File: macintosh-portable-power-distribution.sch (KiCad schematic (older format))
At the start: 23 parts, among them Q1 IRF9Z30, Q10 IRF9020, Q11 IRF9020, Q13 IRF9020, Q14 IRF9Z30, Q15 IRF9Z30, Q16 IRF9Z30, Q2 IRF9020, Q20 IRF9Z30, Q24 702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

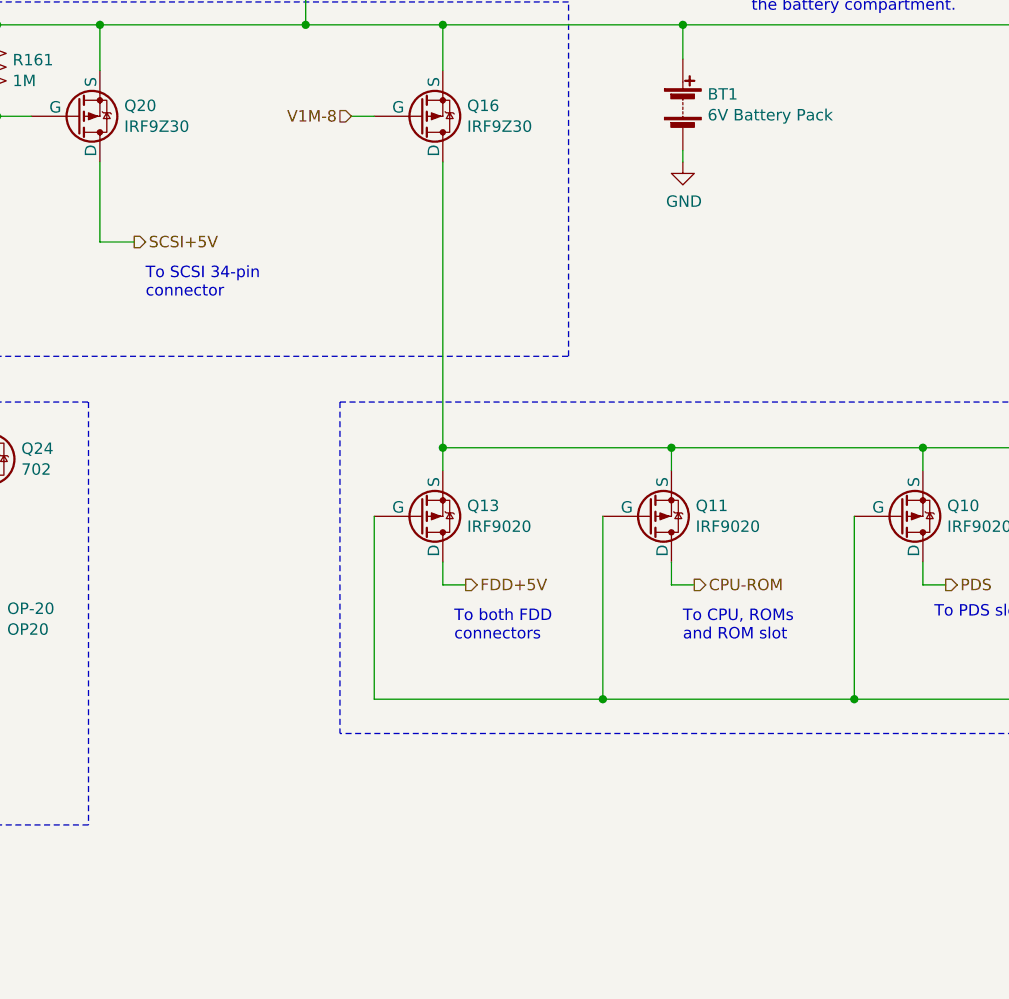
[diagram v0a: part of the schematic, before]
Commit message: Added secondary stage output and RAM output
Signed-off-by: Pawel Pieczul <pieczul@gmail.com>
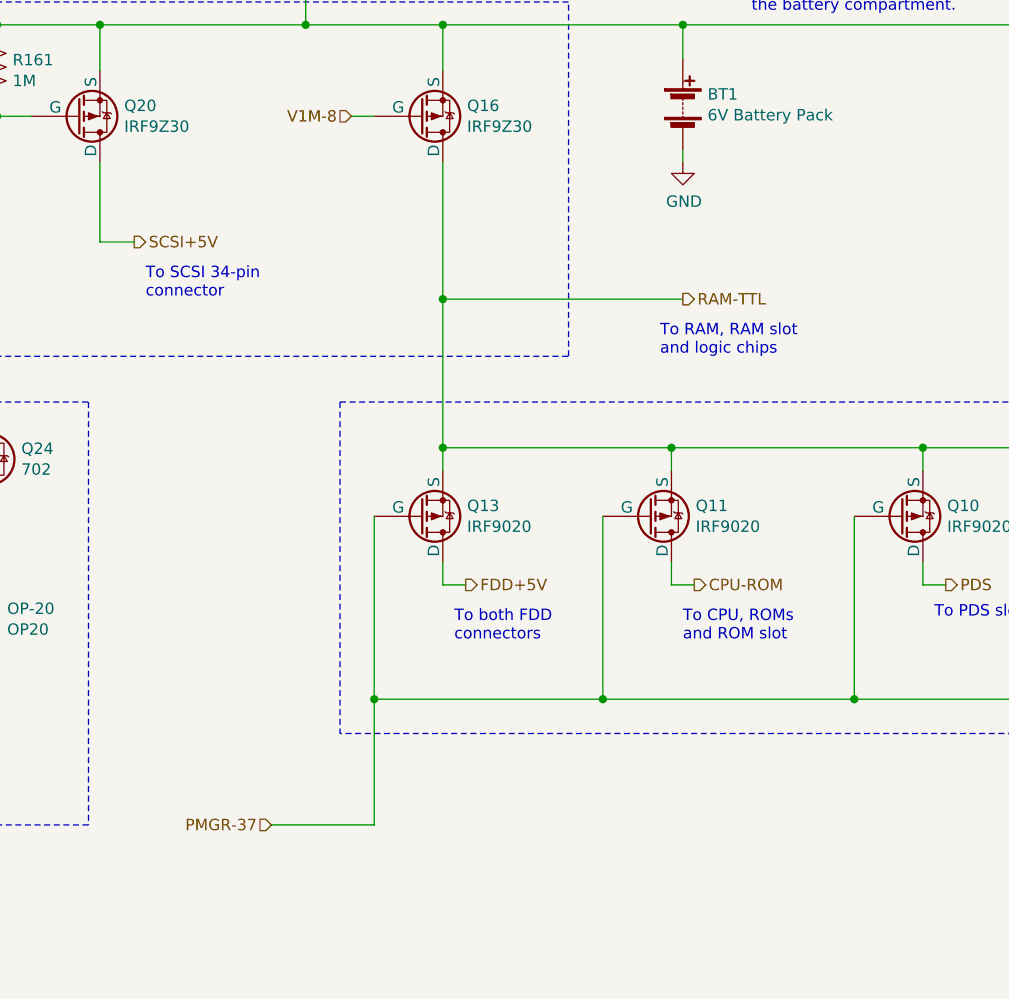
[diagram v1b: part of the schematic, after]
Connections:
- net RAM-TTL: now reaches Q10.3 (S), Q11.3 (S), Q13.3 (S), Q16.2 (D), Q2.3 (S), Q4.3 (S)
- net PMGR-37: now reaches Q10.1 (G), Q11.1 (G), Q13.1 (G), Q4.1 (G)
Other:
- note added: "To RAM, RAM slot\nand logic chips"
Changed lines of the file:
@@
 Title "Macintosh Portable Power Distribution"
 Date "2019-05-22"
-Rev "0.1"
+Rev "0.11"
 Comp "https://oldcrap.org"
 Comment1 ""
@@
 	5750 4650 5750 6100
 Wire Wire Line
-	6200 3600 6200 4850
+	6200 3600 6200 4200
 $Comp
 L Device:Battery BT1
@@
 Text Notes 900  7450 0    50   ~ 0
 V1M - voltage control module, location 1-4M\nPMGR - power management chip, location H15
+Text HLabel 7250 4200 2    50   Output ~ 0
+RAM-TTL
+Wire Wire Line
+	7250 4200 6200 4200
+Connection ~ 6200 4200
+Wire Wire Line
+	6200 4200 6200 4850
+Text Notes 7150 4450 0    50   ~ 0
+To RAM, RAM slot\nand logic chips
+Text HLabel 5450 6500 0    50   Input ~ 0
+PMGR-37
+Wire Wire Line
+	5450 6500 5900 6500
+Wire Wire Line
+	5900 6500 5900 5950
+Connection ~ 5900 5950
 $EndSCHEMATC

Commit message: Added V1M module.
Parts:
- added C16: 100uF, symbol Device:CP1
- added C26, C?: 47uF, symbol Device:CP1
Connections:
- net V1M-41: now also C16.2
- net V1M-51: now also C26.1
- new net: C26.2, C?.2
- new net V1M-39: C16.1
- new net V1M-52: C?.1
- no-connect marks 0 -> 2
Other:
- moved on the sheet: R160
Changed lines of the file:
@@
 $Descr A4 11693 8268
 encoding utf-8
-Sheet 2 3
+Sheet 2 4
 Title "Macintosh Portable Power Distribution"
 Date "2019-05-22"
@@
 L Device:R_US R160
 U 1 1 5CE60BCC
-P 2700 5700
-F 0 "R160" V 2495 5700 50  0000 C CNN
-F 1 "75k" V 2586 5700 50  0000 C CNN
-F 2 "" V 2740 5690 50  0001 C CNN
-F 3 "~" H 2700 5700 50  0001 C CNN
-	1    2700 5700
+P 2850 5700
+F 0 "R160" V 2645 5700 50  0000 C CNN
+F 1 "75k" V 2736 5700 50  0000 C CNN
+F 2 "" V 2890 5690 50  0001 C CNN
+F 3 "~" H 2850 5700 50  0001 C CNN
+	1    2850 5700
 	0    1    1    0
 $EndComp
 Wire Wire Line
-	2850 5700 3200 5700
+	3000 5700 3200 5700
 Connection ~ 3200 5700
 Text HLabel 2400 5700 0    50   Input ~ 0
 V1M-51
 Wire Wire Line
-	2550 5700 2400 5700
+	2700 5700 2550 5700
 Wire Wire Line
 	3200 6000 3200 6050
@@
 Wire Notes Line
 	1850 6500 1850 4650
-Text Notes 1950 6400 0    50   ~ 0
+Text Notes 3650 6400 0    50   ~ 0
 SCSI power enable logic
 Text Notes 4900 4200 0    50   ~ 0
@@
 	5900 6500 5900 5950
 Connection ~ 5900 5950
+Text HLabel 2400 7050 0    50   Input ~ 0
+V1M-52
+$Comp
+L Device:CP1 C26
+U 1 1 5CEA6F81
+P 2550 6050
+F 0 "C26" H 2665 6096 50  0000 L CNN
+F 1 "47uF" H 2665 6005 50  0000 L CNN
+F 2 "" H 2550 6050 50  0001 C CNN
+F 3 "~" H 2550 6050 50  0001 C CNN
+	1    2550 6050
+	1    0    0    -1
+$EndComp
+Wire Wire Line
+	2550 5900 2550 5700
+Connection ~ 2550 5700
+Wire Wire Line
+	2550 5700 2400 5700
+$Comp
+L Device:CP1 C?
+U 1 1 5CEB228F
+P 2550 6750
+F 0 "C?" H 2435 6704 50  0000 R CNN
+F 1 "47uF" H 2435 6795 50  0000 R CNN
+F 2 "" H 2550 6750 50  0001 C CNN
+F 3 "~" H 2550 6750 50  0001 C CNN
+	1    2550 6750
+	-1   0    0    1
+$EndComp
+Wire Wire Line
+	2550 7050 2400 7050
+Wire Wire Line
+	2550 6900 2550 7050
+Wire Wire Line
+	2550 6600 2550 6200
+Text HLabel 9550 1400 2    50   Output ~ 0
+V1M-39
+Text HLabel 9550 1950 2    50   Output ~ 0
+V1M-41
+$Comp
+L Device:CP1 C16
+U 1 1 5CF544A6
+P 9150 1700
+F 0 "C16" H 9265 1746 50  0000 L CNN
+F 1 "100uF" H 9265 1655 50  0000 L CNN
+F 2 "" H 9150 1700 50  0001 C CNN
+F 3 "~" H 9150 1700 50  0001 C CNN
+	1    9150 1700
+	1    0    0    -1
+$EndComp
+Wire Wire Line
+	9150 1550 9150 1400
+Wire Wire Line
+	9150 1400 9550 1400
+Wire Wire Line
+	9150 1850 9150 1950
+Wire Wire Line
+	9150 1950 9550 1950
+NoConn ~ 3950 5900
+NoConn ~ 4050 5900
 $EndSCHEMATC

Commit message: Finished V1M, more references on other sheets.
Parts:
- added C107: 1A4, symbol Device:C
- added C108, C109: 1A5, symbol Device:C
- added Q8: P2A, symbol Device:Q_PNP_BCE
- added Q9: 702, Package_TO_SOT_SMD:TO-252-3_TabPin2, symbol Transistor_FET:IRF9020
- added R101: 100k, symbol Device:R_US
- added R151: 1k, symbol Device:R_US
- added R158, R159: 2.2k, symbol Device:R_US
- C110: value ? -> 1A4
- Q25: value Q_NPN_BCE -> U92
- gave numbers to parts that had none: 1
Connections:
- net GND: now also C107.2, C108.2, C109.2
- net RAM-TTL: now also Q8.3 (E)
- net V1M-25: now also R159.2
- net at Q2.1 (G): now also R26.2; no longer R26.1
- net SERIAL renamed SERIAL-VCC
- new net: C109.1, R158.2, R159.1
- new net: Q8.2 (C), Q9.1 (G), R101.1
- new net: Q8.1 (B), R26.1
- new net J21-31: C107.1, R151.1
- new net J9-10: Q9.3 (S), R101.2
- new net SERIAL-VEE: Q9.2 (D)
- new net V1M-16: C108.1, R158.1
- new net V1M-62: R151.2
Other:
- note added: "Modem\npin 10\n"
- note added: "To 26LS3x (Vcc)"
- note added: "To 26LS3x (Vee)"
- note removed: "?"
- note removed: "To 26LS3x chips\n(ADB, serial I/O)"
- moved on the sheet: BT1, BT2, C110, C16, Q1, Q2, R157

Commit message: Symbol library cleanup
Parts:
- added C102, C103: 1A4, symbol Device:C
- added R147: 100k, symbol Device:R_US
- Q10, Q11, Q13, Q2, Q4: symbol Transistor_FET:IRF9020 -> macintosh-portable:IRF9020
- Q24: symbol Transistor_FET:702 -> macintosh-portable:702
- Q9: symbol Transistor_FET:IRF9020 -> macintosh-portable:702
- renumbered C16 to C18
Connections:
- net labels added: PMGR-45, PMGR-55, PMGR-56, V1M-29, V1M-31, V1M-37, V1M-40
- net labels removed: V1M-39
- wire segments 124 -> 138
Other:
- moved on the sheet: C107, C18, R151

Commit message: Progress on PMGR chip
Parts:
- removed C102, C103, C107: 1A4, symbol Device:C
- removed C18: 100uF, symbol Device:CP1
- removed R147: 100k, symbol Device:R_US
- removed R151: 1k, symbol Device:R_US
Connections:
- net labels added: PMGR-P0-2, PMGR-P0-7, PMGR-VCC
- net labels removed: J21-31, PMGR-37, PMGR-42, PMGR-45, PMGR-52, PMGR-55, PMGR-56, V1M-29, V1M-31, V1M-37, V1M-40, V1M-62
- wire segments 138 -> 116
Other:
- note added: "Enable power to\nRAM, RAM slot, \nlogic chips and PMGR"
- note removed: "To RAM, RAM slot\nand logic chips"
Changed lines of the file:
@@
 $Descr A4 11693 8268
 encoding utf-8
-Sheet 2 5
+Sheet 5 5
 Title "Macintosh Portable Power Distribution"
-Date "2019-05-27"
-Rev "0.12"
+Date "2019-06-08"
+Rev "0.13"
 Comp "https://oldcrap.org"
 Comment1 "Author: Pawel Pieczul"
@@
 V1M-51
 Wire Wire Line
-	2700 5700 2550 5700
-Wire Wire Line
 	3200 6000 3200 6050
 $Comp
@@
 	2850 5100 2900 5100
 Text HLabel 2400 5100 0    50   Input ~ 0
-PMGR-42
+PMGR-P0-2
 Wire Wire Line
 	2400 5100 2550 5100
@@
 V1M - voltage control module, location 1-4M\nPMGR - power management chip, location H15
 Text HLabel 5450 6500 0    50   Input ~ 0
-PMGR-37
+PMGR-P0-7
 Wire Wire Line
 	5450 6500 5900 6500
@@
 	5900 6500 5900 5950
 Connection ~ 5900 5950
-Text HLabel 2400 7050 0    50   Input ~ 0
-V1M-52
-$Comp
-L Device:CP1 C26
-U 1 1 5CEA6F81
-P 2550 6050
-F 0 "C26" H 2665 6096 50  0000 L CNN
-F 1 "47uF" H 2665 6005 50  0000 L CNN
-F 2 "" H 2550 6050 50  0001 C CNN
-F 3 "~" H 2550 6050 50  0001 C CNN
-	1    2550 6050
-	1    0    0    -1
-$EndComp
-Wire Wire Line
-	2550 5900 2550 5700
-Connection ~ 2550 5700
-Wire Wire Line
-	2550 5700 2400 5700
-$Comp
-L Device:CP1 C25
-U 1 1 5CEB228F
-P 2550 6750
-F 0 "C25" H 2435 6704 50  0000 R CNN
-F 1 "47uF" H 2435 6795 50  0000 R CNN
-F 2 "" H 2550 6750 50  0001 C CNN
-F 3 "~" H 2550 6750 50  0001 C CNN
-	1    2550 6750
-	-1   0    0    1
-$EndComp
-Wire Wire Line
-	2550 7050 2400 7050
-Wire Wire Line
-	2550 6900 2550 7050
-Wire Wire Line
-	2550 6600 2550 6200
 NoConn ~ 3950 5900
 NoConn ~ 4050 5900
@@
 Wire Wire Line
 	5600 1950 6000 1950
-$Comp
-L Device:R_US R?
-U 1 1 5DEE1891
-P 9500 900
-AR Path="/5DD4174A/5DEE1891" Ref="R?"  Part="1"
-AR Path="/5CE45908/5DEE1891" Ref="R151"  Part="1"
-F 0 "R151" V 9295 900 50  0000 C CNN
-F 1 "1k" V 9386 900 50  0000 C CNN
-F 2 "" V 9540 890 50  0001 C CNN
-F 3 "~" H 9500 900 50  0001 C CNN
-	1    9500 900
-	0    1    1    0
-$EndComp
-Text HLabel 9250 900  0    50   Input ~ 0
-V1M-62
-Wire Wire Line
-	9250 900  9350 900
-$Comp
-L Device:C C?
-U 1 1 5DEE8ED4
-P 9750 1050
-AR Path="/5DD4174A/5DEE8ED4" Ref="C?"  Part="1"
-AR Path="/5CE45908/5DEE8ED4" Ref="C107"  Part="1"
-F 0 "C107" H 9865 1096 50  0000 L CNN
-F 1 "1A4" H 9865 1005 50  0000 L CNN
-F 2 "" H 9788 900 50  0001 C CNN
-F 3 "~" H 9750 1050 50  0001 C CNN
-	1    9750 1050
-	1    0    0    -1
-$EndComp
-$Comp
-L power:GND #PWR?
-U 1 1 5DEE97A8
-P 9750 1200
-AR Path="/5DD4174A/5DEE97A8" Ref="#PWR?"  Part="1"
-AR Path="/5CE45908/5DEE97A8" Ref="#PWR?"  Part="1"
-F 0 "#PWR?" H 9750 950 50  0001 C CNN
-F 1 "GND" H 9755 1027 50  0000 C CNN
-F 2 "" H 9750 1200 50  0001 C CNN
-F 3 "" H 9750 1200 50  0001 C CNN
-	1    9750 1200
-	1    0    0    -1
-$EndComp
-Wire Wire Line
-	9650 900  9750 900
-Text HLabel 10500 900  2    50   Output ~ 0
-J21-31
-Wire Wire Line
-	9750 900  10200 900
-Connection ~ 9750 900
-Text HLabel 10500 1150 2    50   Output ~ 0
-PMGR-52
-Wire Wire Line
-	10200 900  10200 1150
-Wire Wire Line
-	10200 1150 10500 1150
-Connection ~ 10200 900
-Wire Wire Line
-	10200 900  10500 900
 Text HLabel 9600 3550 0    50   Input ~ 0
 V1M-33
@@
 Wire Notes Line
 	1850 4450 6750 4450
-Text Notes 7000 4550 0    50   ~ 0
-To RAM, RAM slot\nand logic chips
+Text Notes 7150 4600 0    50   ~ 0
+Enable power to\nRAM, RAM slot, \nlogic chips and PMGR
 Wire Wire Line
 	7250 3900 7050 3900
@@
 Text HLabel 3000 3650 0    50   Input ~ 0
 V1M-41
-Wire Wire Line
-	10100 2250 10500 2250
-Wire Wire Line
-	10100 2150 10100 2250
-Wire Wire Line
-	10100 1700 10500 1700
-Wire Wire Line
-	10100 1850 10100 1700
-$Comp
-L Device:CP1 C18
-U 1 1 5CF544A6
-P 10100 2000
-F 0 "C18" H 10215 2046 50  0000 L CNN
-F 1 "100uF" H 10215 1955 50  0000 L CNN
-F 2 "" H 10100 2000 50  0001 C CNN
-F 3 "~" H 10100 2000 50  0001 C CNN
-	1    10100 2000
-	1    0    0    -1
-$EndComp
-Text HLabel 10500 2250 2    50   Output ~ 0
-V1M-31
-Text HLabel 10500 1700 2    50   Output ~ 0
-V1M-29
-$Comp
-L Device:R_US R147
-U 1 1 5D12FA45
-P 3850 2200
-F 0 "R147" V 3645 2200 50  0000 C CNN
-F 1 "100k" V 3736 2200 50  0000 C CNN
-F 2 "" V 3890 2190 50  0001 C CNN
-F 3 "~" H 3850 2200 50  0001 C CNN
-	1    3850 2200
-	-1   0    0    1
-$EndComp
-Text HLabel 4100 1950 2    50   Output ~ 0
-V1M-40
-$Comp
-L Device:C C102
-U 1 1 5D1473B8
-P 3450 2200
-F 0 "C102" H 3565 2246 50  0000 L CNN
-F 1 "1A4" H 3565 2155 50  0000 L CNN
-F 2 "" H 3488 2050 50  0001 C CNN
-F 3 "~" H 3450 2200 50  0001 C CNN
-	1    3450 2200
-	1    0    0    -1
-$EndComp
-Wire Wire Line
-	3850 2050 3850 1950
-Wire Wire Line
-	3850 1950 4100 1950
-Wire Wire Line
-	3450 2050 3450 1950
-Wire Wire Line
-	3450 1950 3850 1950
-Connection ~ 3850 1950
-$Comp
-L power:GND #PWR?
-U 1 1 5D15188C
-P 3850 2350
-AR Path="/5DD4174A/5D15188C" Ref="#PWR?"  Part="1"
-AR Path="/5CE45908/5D15188C" Ref="#PWR?"  Part="1"
-F 0 "#PWR?" H 3850 2100 50  0001 C CNN
-F 1 "GND" H 3855 2177 50  0000 C CNN
-F 2 "" H 3850 2350 50  0001 C CNN
-F 3 "" H 3850 2350 50  0001 C CNN
-	1    3850 2350
-	1    0    0    -1
-$EndComp
-$Comp
-L power:GND #PWR?
-U 1 1 5D152016
-P 3450 2350
-AR Path="/5DD4174A/5D152016" Ref="#PWR?"  Part="1"
-AR Path="/5CE45908/5D152016" Ref="#PWR?"  Part="1"
-F 0 "#PWR?" H 3450 2100 50  0001 C CNN
-F 1 "GND" H 3455 2177 50  0000 C CNN
-F 2 "" H 3450 2350 50  0001 C CNN
-F 3 "" H 3450 2350 50  0001 C CNN
-	1    3450 2350
-	1    0    0    -1
-$EndComp
-Text HLabel 8250 900  2    50   Input ~ 0
-V1M-37
-$Comp
-L Device:C C103
-U 1 1 5D16A202
-P 8050 1150
-F 0 "C103" H 8165 1196 50  0000 L CNN
-F 1 "1A4" H 8165 1105 50  0000 L CNN
-F 2 "" H 8088 1000 50  0001 C CNN
-F 3 "~" H 8050 1150 50  0001 C CNN
-	1    8050 1150
-	1    0    0    -1
-$EndComp
-$Comp
-L power:GND #PWR?
-U 1 1 5D16AB1B
-P 8050 1300
-AR Path="/5DD4174A/5D16AB1B" Ref="#PWR?"  Part="1"
-AR Path="/5CE45908/5D16AB1B" Ref="#PWR?"  Part="1"
-F 0 "#PWR?" H 8050 1050 50  0001 C CNN
-F 1 "GND" H 8055 1127 50  0000 C CNN
-F 2 "" H 8050 1300 50  0001 C CNN
-F 3 "" H 8050 1300 50  0001 C CNN
-	1    8050 1300
-	1    0    0    -1
-$EndComp
-Wire Wire Line
-	8250 900  8050 900
-Wire Wire Line
-	8050 900  8050 1000
-Text HLabel 8300 3900 2    50   Output ~ 0
-PMGR-45
-Text HLabel 8300 4050 2    50   Output ~ 0
-PMGR-55
-Text HLabel 8300 4200 2    50   Output ~ 0
-PMGR-56
+Text HLabel 8250 4350 2    50   Output ~ 0
+PMGR-VCC
 Connection ~ 7050 4050
 Connection ~ 7050 4200
@@
 Wire Wire Line
 	7050 3900 7050 4050
-Wire Wire Line
-	7050 4350 8050 4350
-Wire Wire Line
-	8050 4350 8050 4200
-Wire Wire Line
-	8050 4200 8300 4200
 Connection ~ 7050 4350
 Wire Wire Line
-	8050 4200 8050 4050
-Wire Wire Line
-	8050 4050 8300 4050
-Connection ~ 8050 4200
-Wire Wire Line
-	8050 4050 8050 3900
-Wire Wire Line
-	8050 3900 8300 3900
-Connection ~ 8050 4050
+	7050 4350 8250 4350
+Wire Wire Line
+	2550 6600 2550 6200
+Wire Wire Line
+	2550 5700 2400 5700
+Wire Wire Line
+	2700 5700 2550 5700
+Connection ~ 2550 5700
+Wire Wire Line
+	2550 5900 2550 5700
+$Comp
+L Device:CP1 C26
+U 1 1 5CEA6F81
+P 2550 6050
+F 0 "C26" H 2665 6096 50  0000 L CNN
+F 1 "47uF" H 2665 6005 50  0000 L CNN
+F 2 "" H 2550 6050 50  0001 C CNN
+F 3 "~" H 2550 6050 50  0001 C CNN
+	1    2550 6050
+	1    0    0    -1
+$EndComp
+Wire Wire Line
+	2550 6900 2550 7050
+Wire Wire Line
+	2550 7050 2400 7050
+$Comp
+L Device:CP1 C25
+U 1 1 5CEB228F
+P 2550 6750
+F 0 "C25" H 2435 6704 50  0000 R CNN
+F 1 "47uF" H 2435 6795 50  0000 R CNN
+F 2 "" H 2550 6750 50  0001 C CNN
+F 3 "~" H 2550 6750 50  0001 C CNN
+	1    2550 6750
+	-1   0    0    1
+$EndComp
+Text HLabel 2400 7050 0    50   Input ~ 0
+V1M-52
 $EndSCHEMATC
